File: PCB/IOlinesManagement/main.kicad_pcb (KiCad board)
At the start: 4 copper layers, 138.4 x 80.3 mm, 156 parts, among them J1 Conn_01x02, K1 HK19F-DCxxV-SHC, K10 HK19F-DCxxV-SHC, K11 HK19F-DCxxV-SHC, K12 HK19F-DCxxV-SHC, K13 HK19F-DCxxV-SHC, K14 HK19F-DCxxV-SHC, K15 HK19F-DCxxV-SHC, K16 HK19F-DCxxV-SHC, K2 HK19F-DCxxV-SHC, K3 HK19F-DCxxV-SHC, K4 HK19F-DCxxV-SHC, K5 HK19F-DCxxV-SHC, K6 HK19F-DCxxV-SHC, K7 HK19F-DCxxV-SHC, K8 HK19F-DCxxV-SHC, K9 HK19F-DCxxV-SHC, Q1 BC817, Q10 BC817, Q11 BC817, Q12 BC817, Q13 BC817, Q14 BC817, Q15 BC817, Q16 BC817, Q2 BC817, Q25 BC327, Q3 BC817, Q34 BC327, Q4 BC817, Q5 BC817, Q51 BC327, Q52 BC327, Q53 BC327, Q54 BC327, Q55 BC327, Q56 BC327, Q57 BC327, Q58 BC327, Q59 BC327, Q6 BC817, Q60 BC327, Q61 BC327, Q62 BC327, Q63 BC327, Q64 BC327, Q7 BC817, Q8 BC817, Q9 BC817, U1 MIC4427, U2 MIC4427, U3 MIC4427, U4 MIC4427, U5 MIC4427, U6 MIC4427, U7 MIC4427, U8 MIC4427

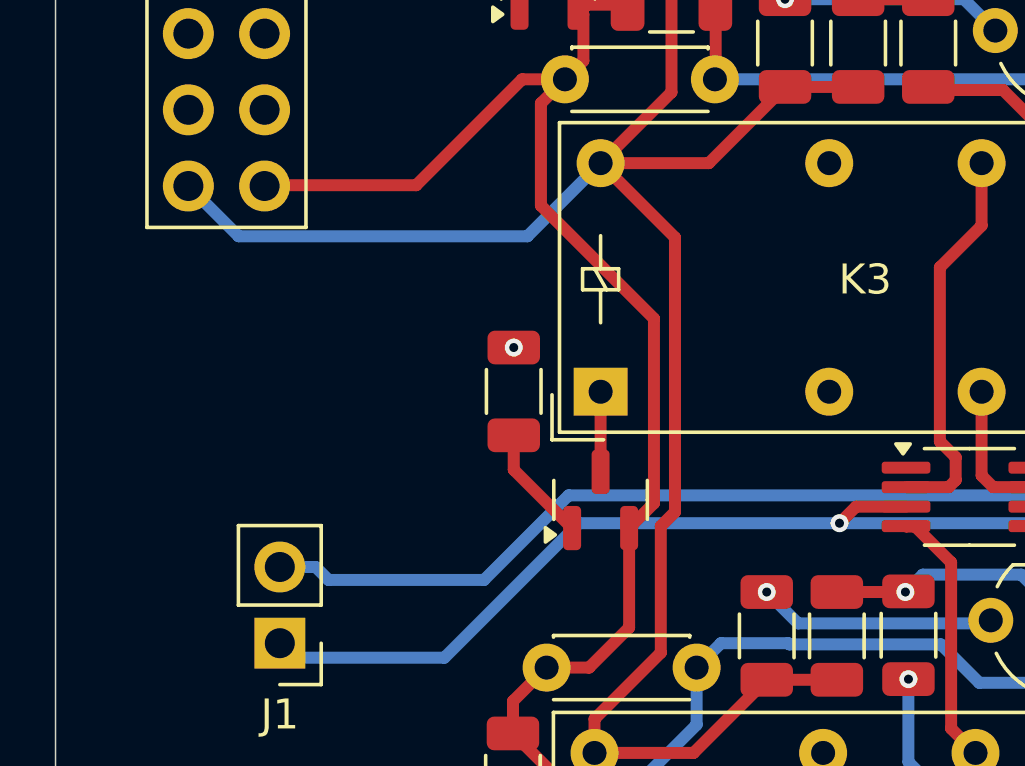
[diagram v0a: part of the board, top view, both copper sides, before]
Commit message: Wrong electric power connection fixed
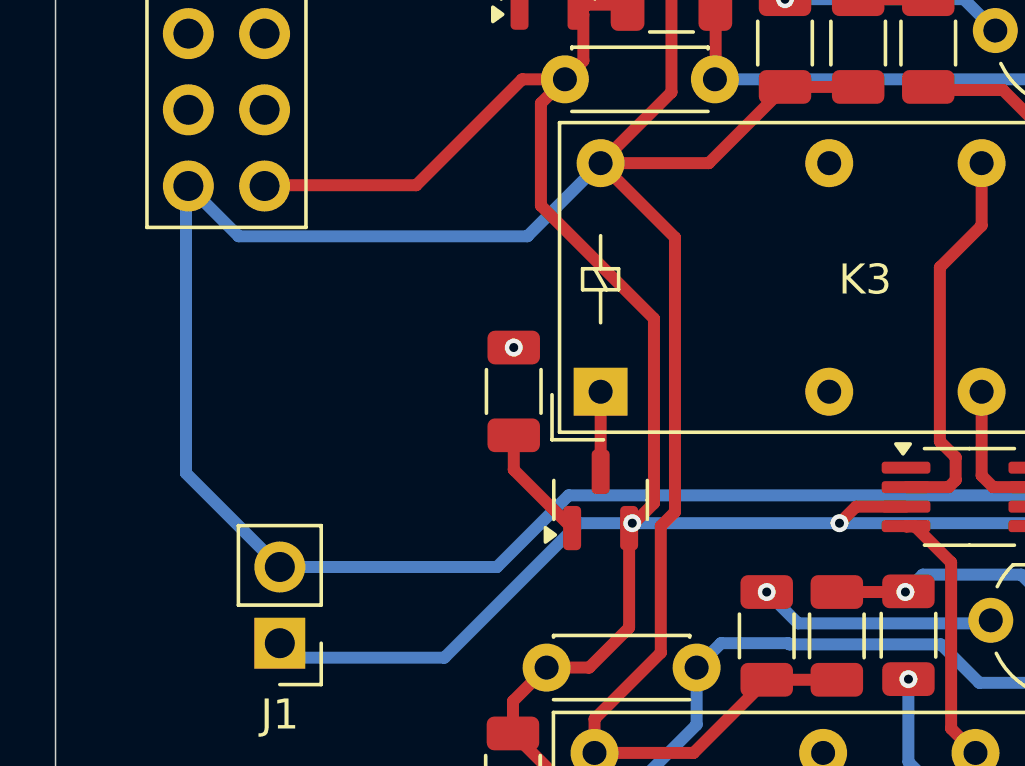
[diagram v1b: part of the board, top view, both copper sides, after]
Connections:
- J1 pad 1: Net-(J1-Pin_1) -> GND
- J1 pad 2: Net-(J1-Pin_2) -> +5V
- U1 pad 3: Net-(J1-Pin_1) -> GND
- U1 pad 6: Net-(J1-Pin_2) -> +5V
- U2 pad 3: Net-(J1-Pin_1) -> GND
- U2 pad 6: Net-(J1-Pin_2) -> +5V
- U3 pad 3: Net-(J1-Pin_1) -> GND
- U3 pad 6: Net-(J1-Pin_2) -> +5V
- U4 pad 3: Net-(J1-Pin_1) -> GND
- U4 pad 6: Net-(J1-Pin_2) -> +5V
- U5 pad 3: Net-(J1-Pin_1) -> GND
- U5 pad 6: Net-(J1-Pin_2) -> +5V
- U6 pad 3: Net-(J1-Pin_1) -> GND
- U6 pad 6: Net-(J1-Pin_2) -> +5V
- U7 pad 3: Net-(J1-Pin_1) -> GND
- U7 pad 6: Net-(J1-Pin_2) -> +5V
- U8 pad 3: Net-(J1-Pin_1) -> GND
- U8 pad 6: Net-(J1-Pin_2) -> +5V
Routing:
- net +5V: track 562.8 -> 805.7 mm, vias 0 -> 8
- net Net-(J1-Pin_1): track 236.7 -> 0.00 mm, vias 8 -> 0
- net GND: track 536.7 -> 773.4 mm, vias 1 -> 10
- net Net-(J1-Pin_2): track 229.2 -> 0.00 mm, vias 8 -> 0
